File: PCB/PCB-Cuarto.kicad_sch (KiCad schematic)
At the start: 0 parts

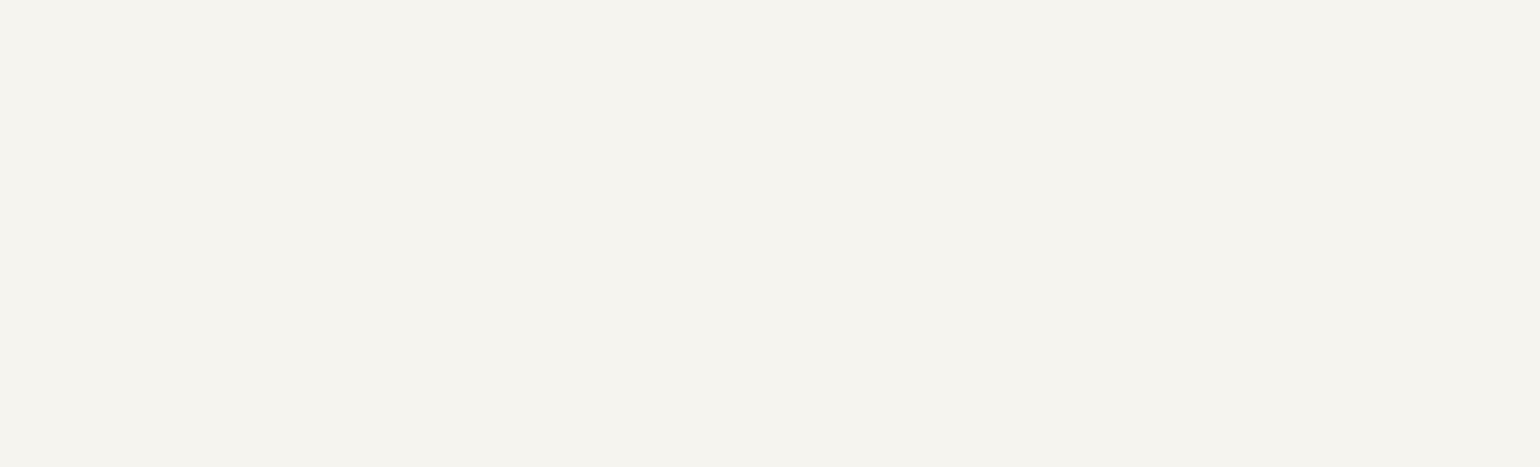
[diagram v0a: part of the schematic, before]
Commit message: Implementacion del eFuse
Se hizo el diseño esquematico del eFuse
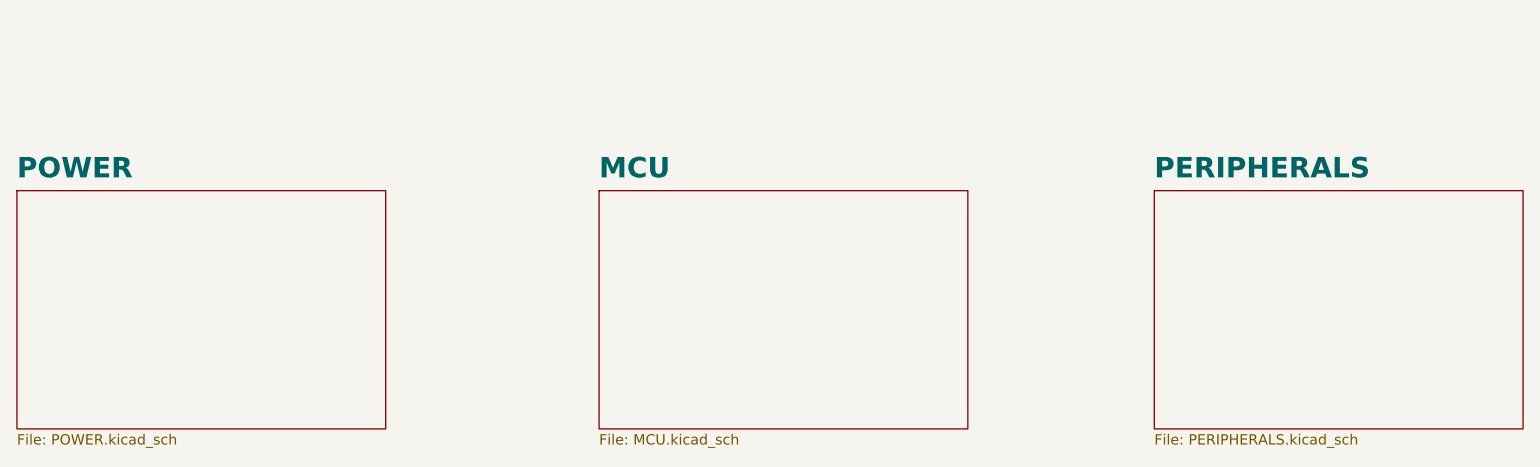
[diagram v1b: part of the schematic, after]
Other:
- added sheet MCU (MCU.kicad_sch)
- added sheet PERIPHERALS (PERIPHERALS.kicad_sch)
- added sheet POWER (POWER.kicad_sch)
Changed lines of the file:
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@@
+		)
+	)
+	(sheet
+		(at 132.588 74.422)
+		(size 45.212 29.21)
+		(fields_autoplaced yes)
+		(stroke
+			(width 0.1524)
+			(type solid)
+		)
+		(fill
+			(color 0 0 0 0.0000)
+		)
+		(property "Sheetname" "MCU"
+			(at 132.588 73.0954 0)
+			(effects
+				(font
+					(size 2.5 2.5)
+					(bold yes)
+				)
+				(justify left bottom)
+			)
+		)
+		(property "Sheetfile" "MCU.kicad_sch"
+			(at 132.588 104.2166 0)
+			(effects
+				(font
+					(size 1.27 1.27)
+				)
+				(justify left top)
+			)
+		)
+		(instances
+			(project "PCB-Cuarto"
+				(path "/118ffa26-3c65-424a-af71-04338c4de0b0"
+					(page "3")
+				)
+			)
+		)
+	)
+	(sheet
+		(at 61.214 74.422)
+		(size 45.212 29.21)
+		(fields_autoplaced yes)
+		(stroke
+			(width 0.1524)
+			(type solid)
+		)
+		(fill
+			(color 0 0 0 0.0000)
+		)
+		(property "Sheetname" "POWER"
+			(at 61.214 73.0954 0)
+			(effects
+				(font
+					(size 2.5 2.5)
+					(bold yes)
+				)
+				(justify left bottom)
+			)
+		)
+		(property "Sheetfile" "POWER.kicad_sch"
+			(at 61.214 104.2166 0)
+			(effects
+				(font
+					(size 1.27 1.27)
+				)
+				(justify left top)
+			)
+		)
+		(instances
+			(project "PCB-Cuarto"
+				(path "/118ffa26-3c65-424a-af71-04338c4de0b0"
+					(page "2")
+				)
+			)
+		)
+	)
+	(sheet
+		(at 200.66 74.422)
+		(size 45.212 29.21)
+		(fields_autoplaced yes)
+		(stroke
+			(width 0.1524)
+			(type solid)
+		)
+		(fill
+			(color 0 0 0 0.0000)
+		)
+		(property "Sheetname" "PERIPHERALS"
+			(at 200.66 73.0954 0)
+			(effects
+				(font
+					(size 2.5 2.5)
+					(bold yes)
+				)
+				(justify left bottom)
+			)
+		)
+		(property "Sheetfile" "PERIPHERALS.kicad_sch"
+			(at 200.66 104.2166 0)
+			(effects
+				(font
+					(size 1.27 1.27)
+				)
+				(justify left top)
+			)
+		)
+		(instances
+			(project "PCB-Cuarto"
+				(path "/118ffa26-3c65-424a-af71-04338c4de0b0"
+					(page "4")
+				)
+			)
 		)
 	)

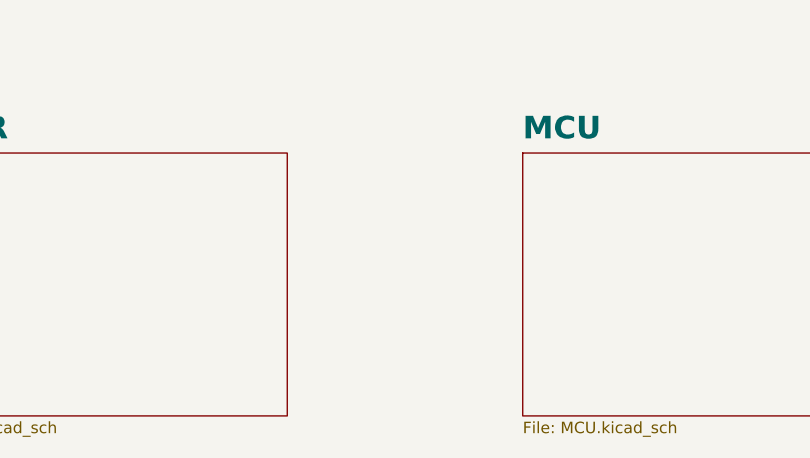
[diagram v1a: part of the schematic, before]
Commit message: Diseño MCU ESP32-S3 y USB-C conector
Se diseño el ESP32-S3-WROOM-1 junto a su conector USB-C para flashear el MCU
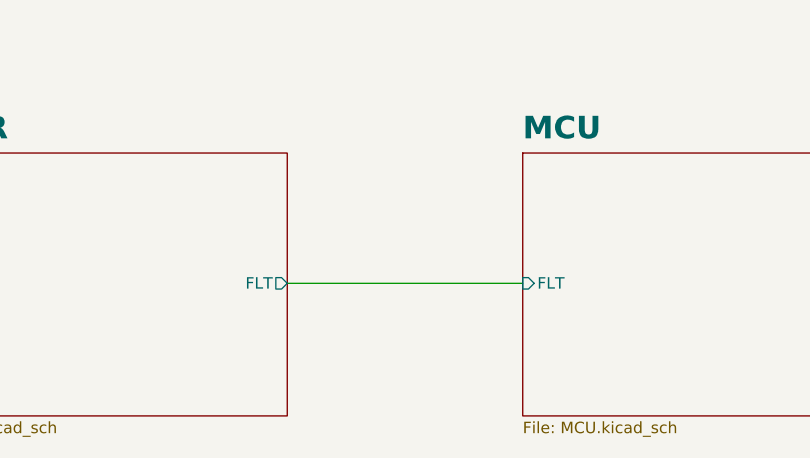
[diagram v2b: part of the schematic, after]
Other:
- sheet MCU ports: added FLT; removed none
- sheet POWER ports: added FLT; removed none
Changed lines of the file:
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@@
 	(generator_version "8.0")
 	(paper "A4")
+	(wire
+		(pts
+			(xy 106.426 88.9) (xy 132.588 88.9)
+		)
+		(stroke
+			(width 0)
+			(type default)
+		)
+	)
 	(text "- ENTRADA DE ALIMENTACION 24V\n- CONTROL DE CHAPA DE 12V@0.2A\n- CONEXION RS485 EN FORMATO DAYSI CHAIN\n- UPDATE DEL FIRMWARE POR OTTA\n- CONECTORES DEBEN RECIBIR HASTA CABLE 12"
 		(exclude_from_sim no)
@@
 			)
 		)
+		(pin "FLT" input
+			(at 132.588 88.9 180)
+			(effects
+				(font
+					(size 1.27 1.27)
+				)
+				(justify left)
+			)
+		)
 		(instances
 			(project "PCB-Cuarto"
@@
 			)
 		)
+		(pin "FLT" output
+			(at 106.426 88.9 0)
+			(effects
+				(font
+					(size 1.27 1.27)
+				)
+				(justify right)
+			)
+		)

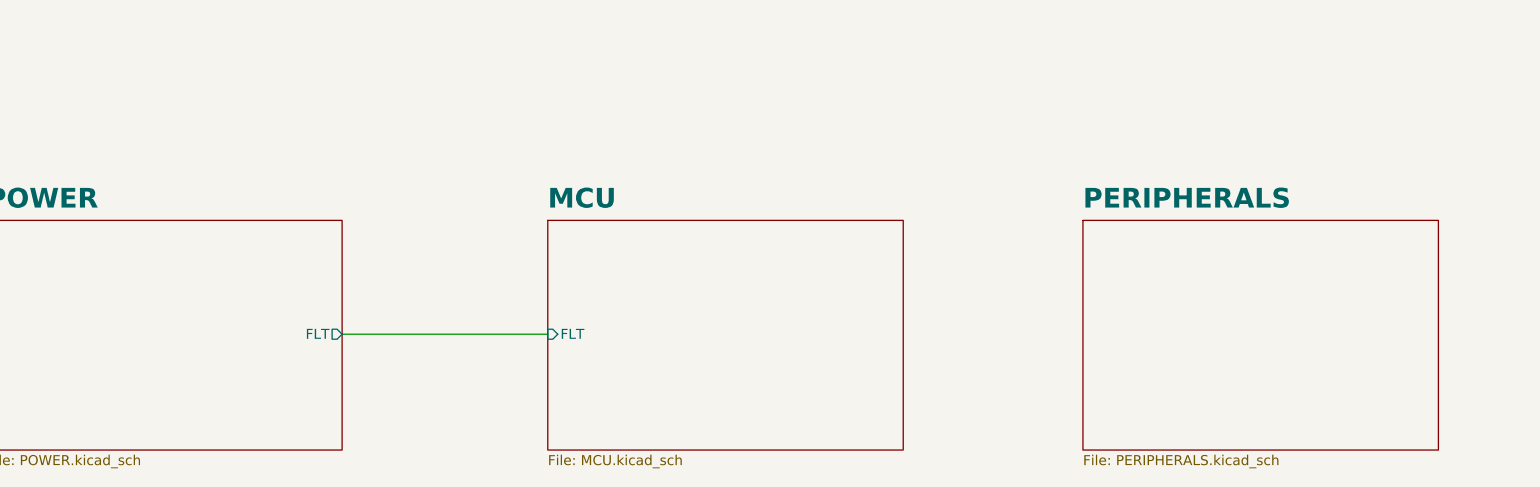
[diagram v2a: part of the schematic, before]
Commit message: Agregado RS485, Smart Switch, ORING Diode
Se termino de acabar todo el esquematico, solo falta crear el footprint para un inductor
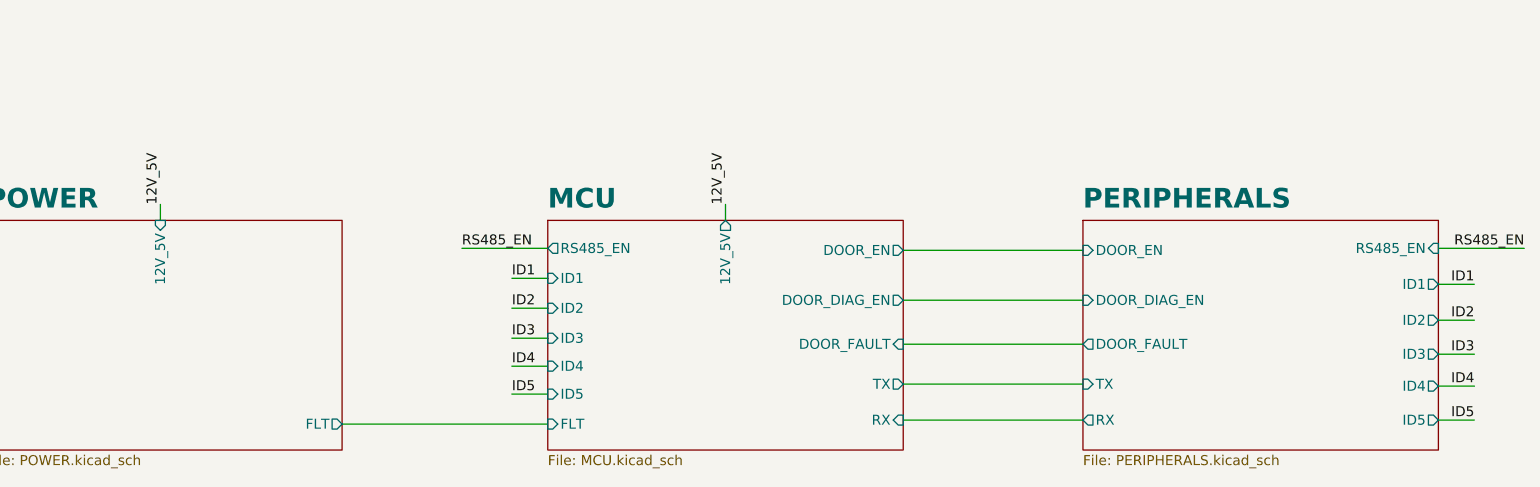
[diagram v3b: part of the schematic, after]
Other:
- sheet MCU ports: added 12V_5V, DOOR_DIAG_EN, DOOR_EN, DOOR_FAULT, ID1, ID2, ID3, ID4, ID5, RS485_EN, RX, TX; removed none
- sheet PERIPHERALS ports: added DOOR_DIAG_EN, DOOR_EN, DOOR_FAULT, ID1, ID2, ID3, ID4, ID5, RS485_EN, RX, TX; removed none
- sheet POWER ports: added 12V_5V; removed none

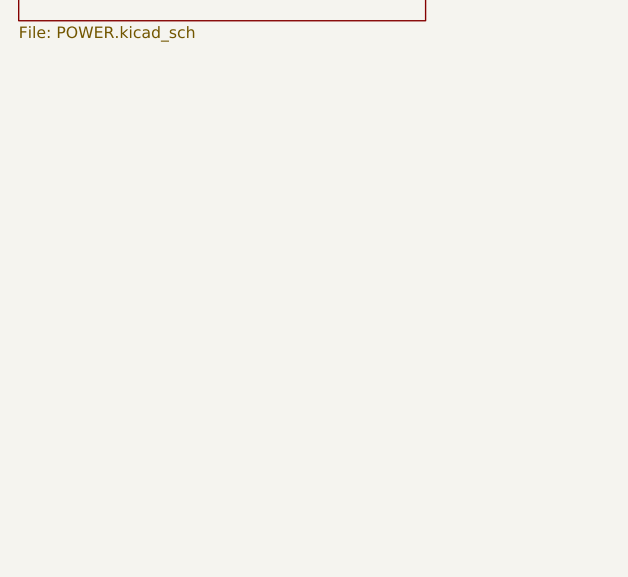
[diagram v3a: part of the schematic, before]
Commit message: Placement
Se termino de crear el footprint para el inductor y placement en la PCB
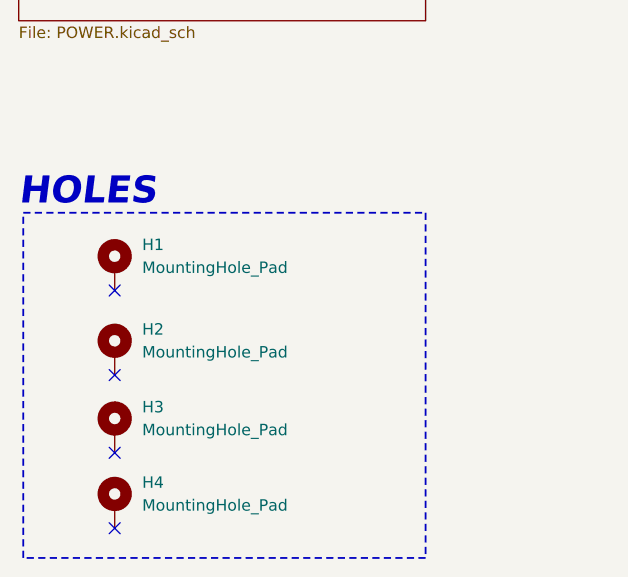
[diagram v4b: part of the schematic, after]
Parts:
- added H1, H2, H3, H4: MountingHole_Pad, MountingHole:MountingHole_3.5mm_Pad_Via, symbol Mechanical:MountingHole_Pad
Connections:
- no-connect marks 0 -> 4
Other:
- note added: "HOLES"
